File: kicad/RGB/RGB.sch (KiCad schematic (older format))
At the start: 13 parts, among them SW1 SW_Push, U1 ATmega16A-AU, Y1 Crystal

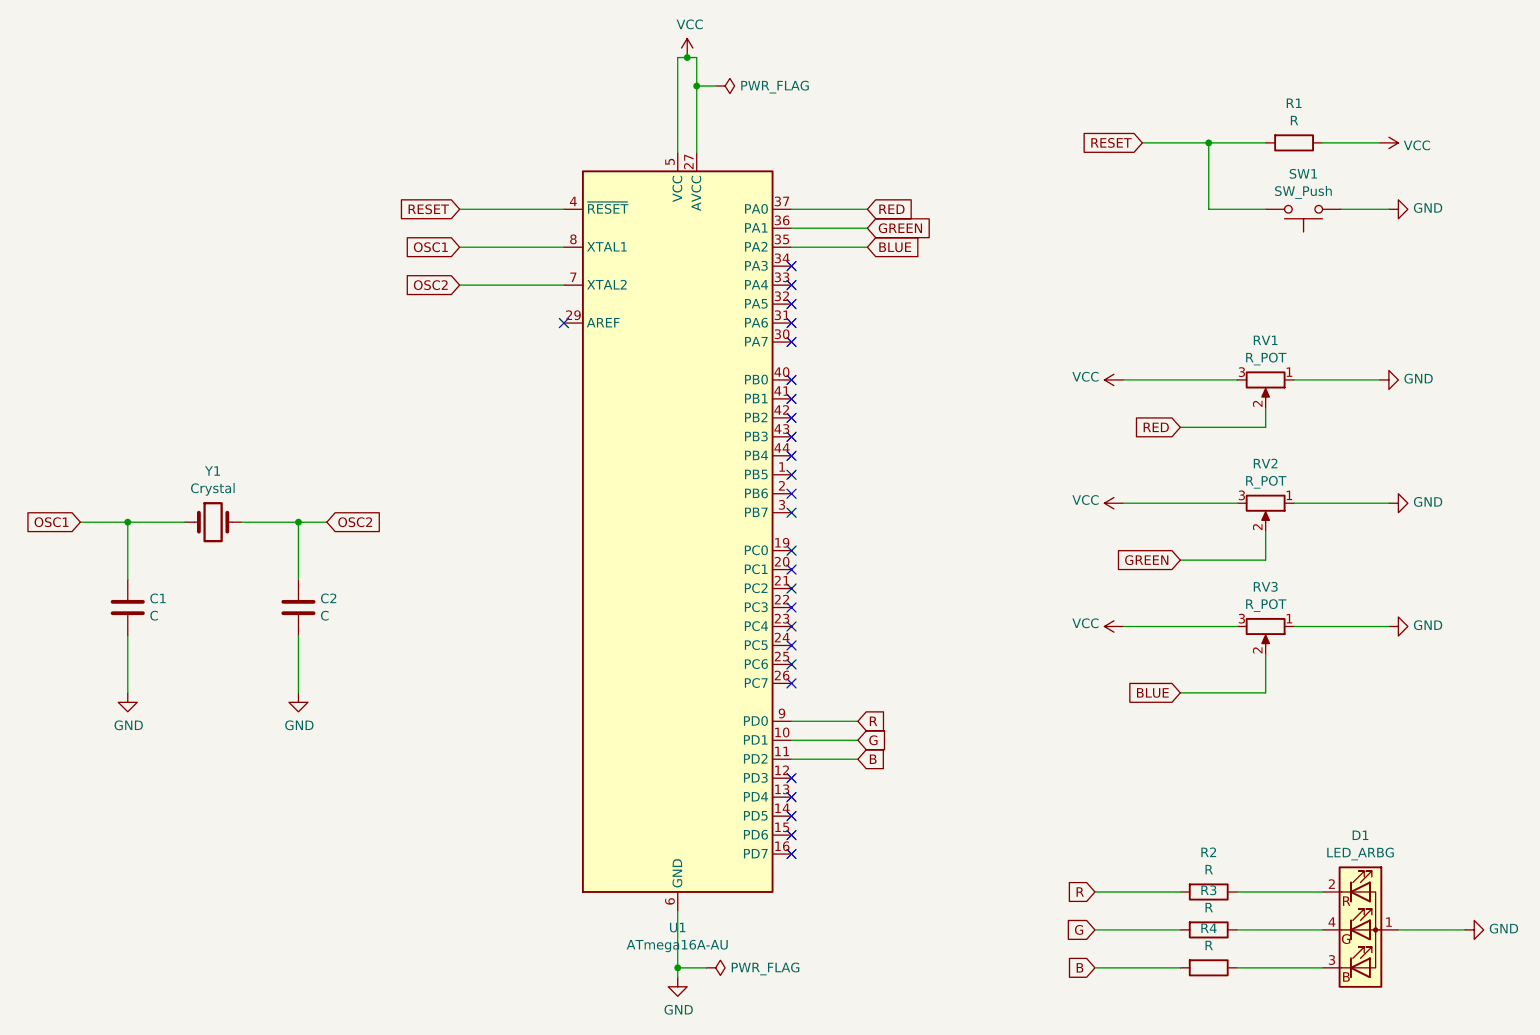
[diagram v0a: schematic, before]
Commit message: Values and power led added. Schema done.
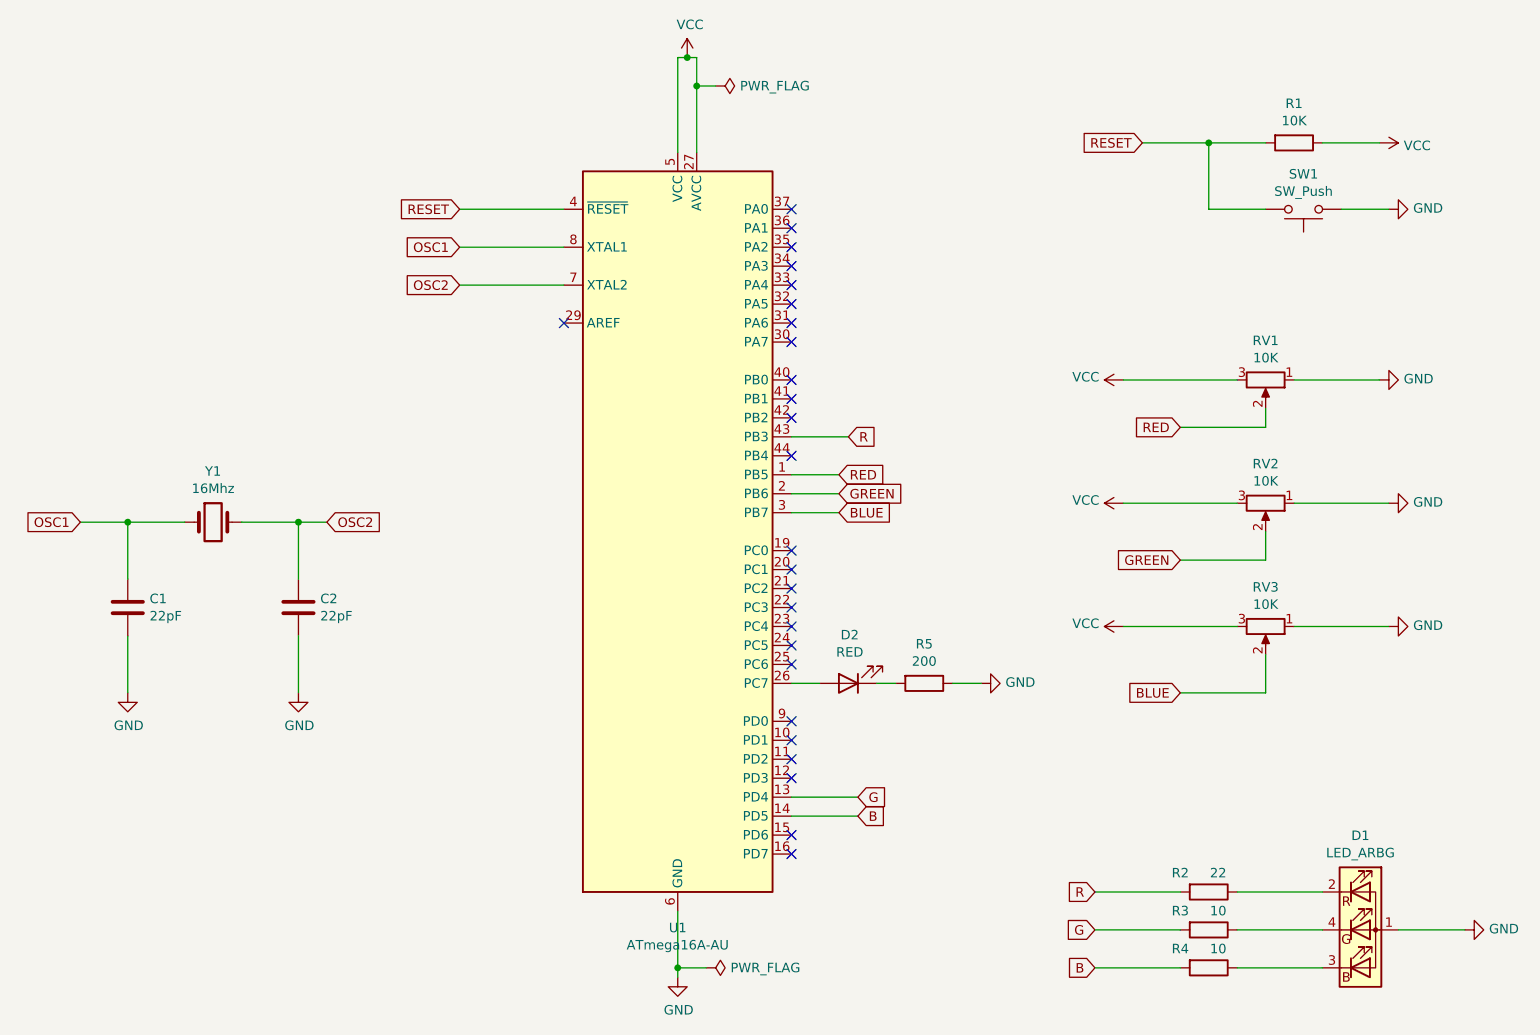
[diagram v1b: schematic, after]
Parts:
- added D2: RED, symbol Device:LED
- added R5: 200, symbol Device:R
- C1, C2: value C -> 22pF
- R1: value R -> 10K
- R2: value R -> 22
- R3, R4: value R -> 10
- RV1, RV2, RV3: value R_POT -> 10K
- Y1: value Crystal -> 16Mhz
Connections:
- net B: now also U1.14 (PD5); no longer U1.11 (PD2)
- net BLUE: now also U1.3 (PB7); no longer U1.35 (PA2)
- net G: now also U1.13 (PD4); no longer U1.10 (PD1)
- net GND: now also R5.1
- net GREEN: now also U1.2 (PB6); no longer U1.36 (PA1)
- net R: now also U1.43 (PB3); no longer U1.9 (PD0)
- net RED: now also U1.1 (PB5); no longer U1.37 (PA0)
- net at U1.26 (PC7): now also D2.2 (A)
- new net: D2.1 (K), R5.2
- no-connect marks 27 -> 26
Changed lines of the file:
@@
 P 7800 1450
 F 0 "R1" V 7593 1450 50  0000 C CNN
-F 1 "R" V 7684 1450 50  0000 C CNN
+F 1 "10K" V 7684 1450 50  0000 C CNN
 F 2 "" V 7730 1450 50  0001 C CNN
 F 3 "~" H 7800 1450 50  0001 C CNN
@@
 P 2100 3450
 F 0 "Y1" H 2100 3718 50  0000 C CNN
-F 1 "Crystal" H 2100 3627 50  0000 C CNN
+F 1 "16Mhz" H 2100 3627 50  0000 C CNN
 F 2 "" H 2100 3450 50  0001 C CNN
 F 3 "~" H 2100 3450 50  0001 C CNN
@@
 P 1650 3900
 F 0 "C1" H 1765 3946 50  0000 L CNN
-F 1 "C" H 1765 3855 50  0000 L CNN
+F 1 "22pF" H 1765 3855 50  0000 L CNN
 F 2 "" H 1688 3750 50  0001 C CNN
 F 3 "~" H 1650 3900 50  0001 C CNN
@@
 P 2550 3900
 F 0 "C2" H 2665 3946 50  0000 L CNN
-F 1 "C" H 2665 3855 50  0000 L CNN
+F 1 "22pF" H 2665 3855 50  0000 L CNN
 F 2 "" H 2588 3750 50  0001 C CNN
 F 3 "~" H 2550 3900 50  0001 C CNN
@@
 P 7650 2700
 F 0 "RV1" V 7443 2700 50  0000 C CNN
-F 1 "R_POT" V 7534 2700 50  0000 C CNN
+F 1 "10K" V 7534 2700 50  0000 C CNN
 F 2 "" H 7650 2700 50  0001 C CNN
 F 3 "~" H 7650 2700 50  0001 C CNN
@@
 P 7650 3350
 F 0 "RV2" V 7443 3350 50  0000 C CNN
-F 1 "R_POT" V 7534 3350 50  0000 C CNN
+F 1 "10K" V 7534 3350 50  0000 C CNN
 F 2 "" H 7650 3350 50  0001 C CNN
 F 3 "~" H 7650 3350 50  0001 C CNN
@@
 P 7650 4000
 F 0 "RV3" V 7443 4000 50  0000 C CNN
-F 1 "R_POT" V 7534 4000 50  0000 C CNN
+F 1 "10K" V 7534 4000 50  0000 C CNN
 F 2 "" H 7650 4000 50  0001 C CNN
 F 3 "~" H 7650 4000 50  0001 C CNN
@@
 U 1 1 60AD70D7
 P 7350 5400
-F 0 "R2" V 7143 5400 50  0000 C CNN
-F 1 "R" V 7234 5400 50  0000 C CNN
+F 0 "R2" V 7250 5250 50  0000 C CNN
+F 1 "22" V 7250 5450 50  0000 C CNN
 F 2 "" V 7280 5400 50  0001 C CNN
 F 3 "~" H 7350 5400 50  0001 C CNN
@@
 U 1 1 60AD76D8
 P 7350 5600
-F 0 "R3" V 7143 5600 50  0000 C CNN
-F 1 "R" V 7234 5600 50  0000 C CNN
+F 0 "R3" V 7250 5450 50  0000 C CNN
+F 1 "10" V 7250 5650 50  0000 C CNN
 F 2 "" V 7280 5600 50  0001 C CNN
 F 3 "~" H 7350 5600 50  0001 C CNN
@@
 U 1 1 60AD7911
 P 7350 5800
-F 0 "R4" V 7143 5800 50  0000 C CNN
-F 1 "R" V 7234 5800 50  0000 C CNN
+F 0 "R4" V 7250 5650 50  0000 C CNN
+F 1 "10" V 7250 5850 50  0000 C CNN
 F 2 "" V 7280 5800 50  0001 C CNN
 F 3 "~" H 7350 5800 50  0001 C CNN
@@
 Wire Wire Line
 	7500 5800 7950 5800
-Text GLabel 5550 1800 2    50   Input ~ 0
+Text GLabel 5400 3200 2    50   Input ~ 0
 RED
-Text GLabel 5550 1900 2    50   Input ~ 0
+Text GLabel 5400 3300 2    50   Input ~ 0
 GREEN
-Text GLabel 5550 2000 2    50   Input ~ 0
+Text GLabel 5400 3400 2    50   Input ~ 0
 BLUE
-Wire Wire Line
-	5150 1800 5550 1800
-Wire Wire Line
-	5150 1900 5550 1900
-Wire Wire Line
-	5150 2000 5550 2000
-Text GLabel 5500 4500 2    50   Input ~ 0
+Text GLabel 5450 3000 2    50   Input ~ 0
 R
-Text GLabel 5500 4600 2    50   Input ~ 0
+Text GLabel 5500 4900 2    50   Input ~ 0
 G
-Text GLabel 5500 4700 2    50   Input ~ 0
+Text GLabel 5500 5000 2    50   Input ~ 0
 B
-Wire Wire Line
-	5150 4500 5500 4500
-Wire Wire Line
-	5150 4600 5500 4600
-Wire Wire Line
-	5150 4700 5500 4700
 $Comp
 L power:GND #PWR012
@@
 NoConn ~ 5150 2800
 NoConn ~ 5150 2900
-NoConn ~ 5150 3000
 NoConn ~ 5150 3100
-NoConn ~ 5150 3200
-NoConn ~ 5150 3300
-NoConn ~ 5150 3400
 NoConn ~ 5150 3600
 NoConn ~ 5150 3700
@@
 NoConn ~ 5150 4100
 NoConn ~ 5150 4200
-NoConn ~ 5150 4300
 NoConn ~ 5150 4800
-NoConn ~ 5150 4900
-NoConn ~ 5150 5000
 NoConn ~ 5150 5100
 NoConn ~ 5150 5200
@@
 	4650 1150 4650 1500
 $Comp
-L power:PWR_FLAG #FLG?
+L power:PWR_FLAG #FLG02
 U 1 1 60B1085B
 P 4700 5800
-F 0 "#FLG?" H 4700 5875 50  0001 C CNN
+F 0 "#FLG02" H 4700 5875 50  0001 C CNN
 F 1 "PWR_FLAG" V 4700 5928 50  0000 L CNN
 F 2 "" H 4700 5800 50  0001 C CNN
@@
 Wire Wire Line
 	4550 5800 4550 5850
+Wire Wire Line
+	5150 5000 5500 5000
+Wire Wire Line
+	5150 4900 5500 4900
+Wire Wire Line
+	5150 3000 5450 3000
+NoConn ~ 5150 4500
+NoConn ~ 5150 4600
+NoConn ~ 5150 4700
+Wire Wire Line
+	5150 3200 5400 3200
+Wire Wire Line
+	5150 3300 5400 3300
+Wire Wire Line
+	5150 3400 5400 3400
+NoConn ~ 5150 1800
+NoConn ~ 5150 1900
+NoConn ~ 5150 2000
+$Comp
+L Device:LED D2
+U 1 1 60B1F77D
+P 5450 4300
+F 0 "D2" H 5443 4045 50  0000 C CNN
+F 1 "RED" H 5443 4136 50  0000 C CNN
+F 2 "" H 5450 4300 50  0001 C CNN
+F 3 "~" H 5450 4300 50  0001 C CNN
+	1    5450 4300
+	-1   0    0    1
+$EndComp
+Wire Wire Line
+	5150 4300 5300 4300
+$Comp
+L Device:R R5
+U 1 1 60B223D3
+P 5850 4300
+F 0 "R5" V 5643 4300 50  0000 C CNN
+F 1 "200" V 5734 4300 50  0000 C CNN
+F 2 "" V 5780 4300 50  0001 C CNN
+F 3 "~" H 5850 4300 50  0001 C CNN
+	1    5850 4300
+	0    1    1    0
+$EndComp
+$Comp
+L power:GND #PWR014
+U 1 1 60B22910
+P 6150 4300
+F 0 "#PWR014" H 6150 4050 50  0001 C CNN
+F 1 "GND" V 6155 4172 50  0000 R CNN
+F 2 "" H 6150 4300 50  0001 C CNN
+F 3 "" H 6150 4300 50  0001 C CNN
+	1    6150 4300
+	0    -1   -1   0
+$EndComp
+Wire Wire Line
+	5600 4300 5700 4300
+Wire Wire Line
+	6000 4300 6150 4300
 $EndSCHEMATC
